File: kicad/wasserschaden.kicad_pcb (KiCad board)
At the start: 2 copper layers, 50.8 x 49.5 mm, 18 parts, among them J1 valve out, J2 12V in, J3 sense, U1 stepdown, U2 WeMos_mini, U3 DS18B20

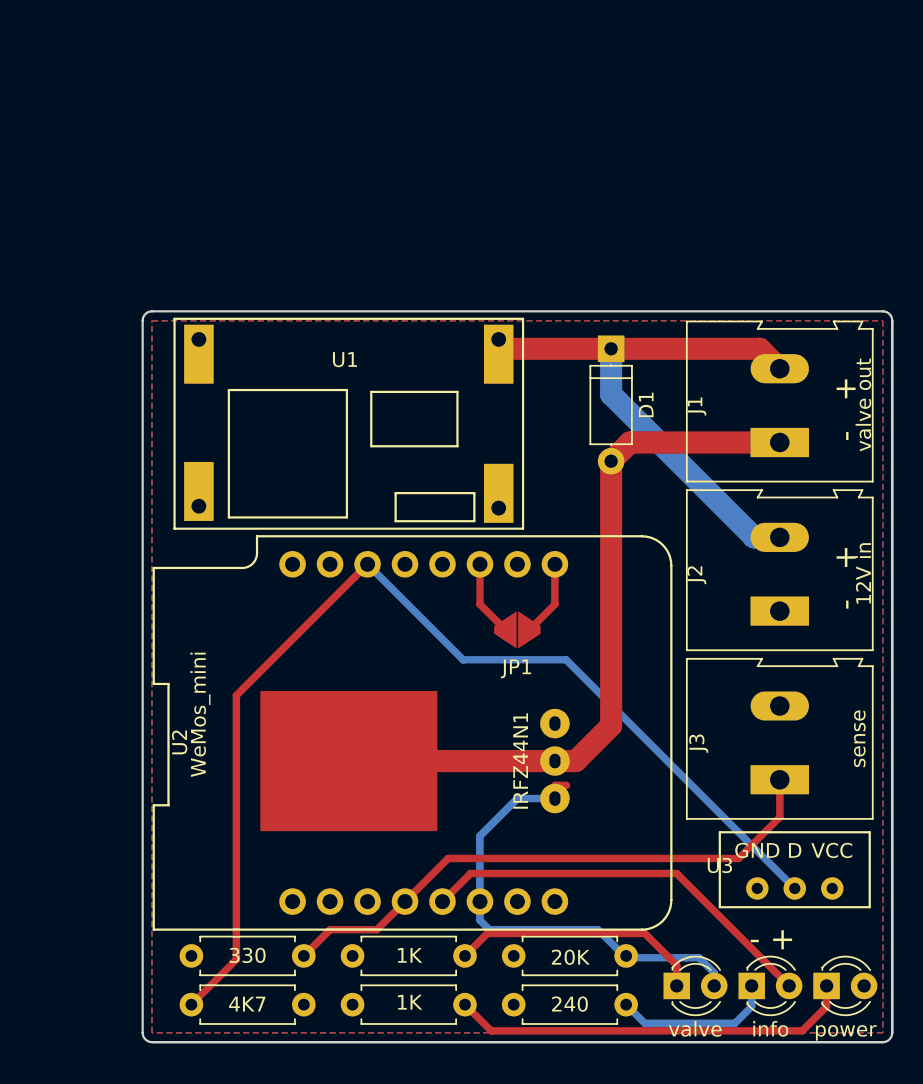
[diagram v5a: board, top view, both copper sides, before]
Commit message: added 12V zone, made screw terminals interlockable
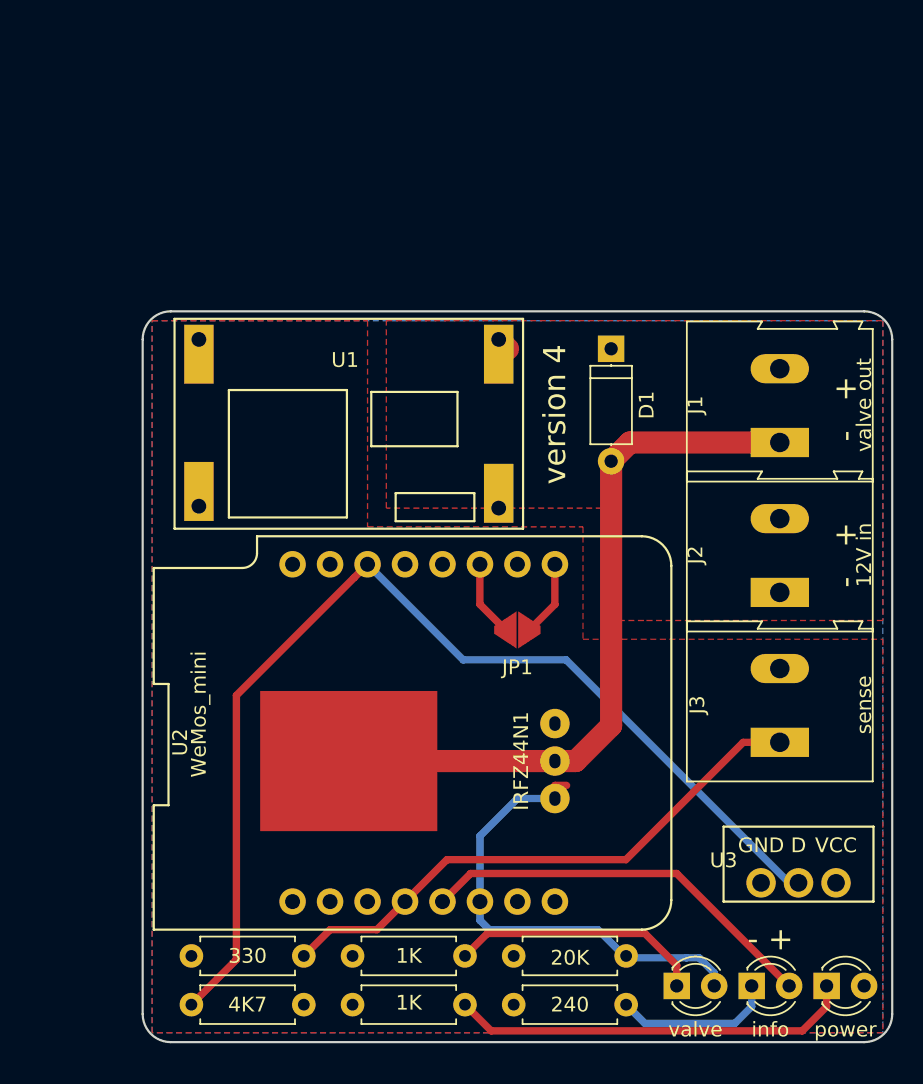
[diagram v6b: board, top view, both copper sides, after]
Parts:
- moved J3 2.54 mm to (168.9, 87.6)
- moved J2 1.27 mm to (168.9, 77.5)
- moved U3 0.46 mm to (170.2, 99.7)
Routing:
- net +12V: track 41.0 -> 3.52 mm
- added copper zone on F.Cu, net +12V
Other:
- outline, holes or cut-outs redrawn
- board text added: "version 4"
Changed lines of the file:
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@@
   (general
     (thickness 1.6)
-    (drawings 13)
-    (tracks 65)
+    (drawings 12)
+    (tracks 59)
     (zones 0)
     (modules 18)
@@
     (mod_text_size 1 1)
     (mod_text_width 0.15)
-    (pad_size 10 12)
-    (pad_drill 3.5)
+    (pad_size 2 2)
+    (pad_drill 1.2)
     (pad_to_mask_clearance 0.2)
     (solder_mask_min_width 0.25)
@@
   )
   (module Connectors_Terminal_Blocks:TerminalBlock_Altech_AK300-2_P5.00mm (layer F.Cu)
-    (at 168.91 78.74 90)
+    (at 168.91 77.47 90)
     (descr "Altech AK300 terminal block, pitch 5.0mm, 45 degree angled, see http://www.mouser.com/ds/2/16/PCBMETRC-24178.pdf")
     (tags "Altech AK300 terminal block pitch 5.0mm")
@@
   )
   (module Connectors_Terminal_Blocks:TerminalBlock_Altech_AK300-2_P5.00mm (layer F.Cu)
-    (at 168.91 90.17 90)
+    (at 168.91 87.63 90)
     (descr "Altech AK300 terminal block, pitch 5.0mm, 45 degree angled, see http://www.mouser.com/ds/2/16/PCBMETRC-24178.pdf")
     (tags "Altech AK300 terminal block pitch 5.0mm")
@@
       (effects (font (size 1 1) (thickness 0.15)))
     )
-    (fp_text value sense (at 2.78 5.334 90) (layer F.SilkS)
+    (fp_text value sense (at 2.54 5.715 90) (layer F.SilkS)
       (effects (font (size 1 1) (thickness 0.15)))
     )
@@
   )
   (module custom:temperature_sensor (layer F.Cu)
-    (at 169.926 100.076)
+    (at 170.18 99.695)
     (fp_text reference U3 (at -5.08 -4.064) (layer F.SilkS)
       (effects (font (size 1 1) (thickness 0.15)))
@@
       (effects (font (size 1 1) (thickness 0.15)))
     )
-    (pad 3 thru_hole circle (at 2.54 -2.54) (size 1.524 1.524) (drill 0.762) (layers *.Cu *.Mask)
+    (pad 3 thru_hole circle (at 2.54 -2.54) (size 2 2) (drill 1.2) (layers *.Cu *.Mask)
       (net 17 +3V3))
-    (pad 2 thru_hole circle (at 0 -2.54) (size 1.524 1.524) (drill 0.762) (layers *.Cu *.Mask)
+    (pad 2 thru_hole circle (at 0 -2.54) (size 2 2) (drill 1.2) (layers *.Cu *.Mask)
       (net 21 "Net-(R6-Pad2)"))
-    (pad 1 thru_hole circle (at -2.54 -2.54) (size 1.524 1.524) (drill 0.762) (layers *.Cu *.Mask)
+    (pad 1 thru_hole circle (at -2.54 -2.54) (size 2 2) (drill 1.2) (layers *.Cu *.Mask)
       (net 3 GND))
   )
-  (gr_arc (start 175.895 107.315) (end 176.53 107.315) (angle 90) (layer Edge.Cuts) (width 0.15))
-  (gr_text "- +" (at 168.402 100.965) (layer F.SilkS)
+  (gr_arc (start 127.635 106.045) (end 125.73 106.045) (angle -90) (layer Edge.Cuts) (width 0.15))
+  (gr_arc (start 174.625 106.045) (end 174.625 107.95) (angle -90) (layer Edge.Cuts) (width 0.15))
+  (gr_arc (start 174.625 60.325) (end 176.53 60.325) (angle -90) (layer Edge.Cuts) (width 0.15))
+  (gr_arc (start 127.635 60.325) (end 127.635 58.42) (angle -90) (layer Edge.Cuts) (width 0.15))
+  (gr_text "version 4" (at 153.67 65.405 90) (layer F.SilkS)
+    (effects (font (size 1.5 1.5) (thickness 0.3)))
+  )
+  (gr_text "- +" (at 168.275 100.965) (layer F.SilkS)
     (effects (font (size 1.5 1.5) (thickness 0.3)))
   )
@@
     (effects (font (size 1.5 1.5) (thickness 0.3)))
   )
-  (gr_text "-   +" (at 173.355 76.454 90) (layer F.SilkS)
+  (gr_text "-   +" (at 173.355 74.93 90) (layer F.SilkS)
     (effects (font (size 1.5 1.5) (thickness 0.3)))
   )
-  (gr_line (start 175.895 107.95) (end 126.365 107.95) (angle 90) (layer Edge.Cuts) (width 0.15))
-  (gr_arc (start 126.365 107.315) (end 126.365 107.95) (angle 90) (layer Edge.Cuts) (width 0.15))
-  (gr_line (start 126.365 107.95) (end 175.895 107.95) (angle 90) (layer Edge.Cuts) (width 0.15))
-  (gr_line (start 176.53 59.055) (end 176.53 107.315) (angle 90) (layer Edge.Cuts) (width 0.15))
-  (gr_arc (start 126.365 59.055) (end 125.73 59.055) (angle 90) (layer Edge.Cuts) (width 0.15))
-  (gr_arc (start 175.895 59.055) (end 175.895 58.42) (angle 90) (layer Edge.Cuts) (width 0.15))
-  (gr_line (start 175.895 58.42) (end 126.365 58.42) (angle 90) (layer Edge.Cuts) (width 0.15))
-  (gr_line (start 176.53 59.055) (end 176.53 107.315) (angle 90) (layer Edge.Cuts) (width 0.15))
-  (gr_line (start 125.73 59.055) (end 125.73 107.315) (angle 90) (layer Edge.Cuts) (width 0.15))
-  (segment (start 157.48 60.96) (end 157.48 64.06) (width 1.5) (layer B.Cu) (net 1))
-  (segment (start 157.48 64.06) (end 167.16 73.74) (width 1.5) (layer B.Cu) (net 1))
-  (segment (start 167.16 73.74) (end 168.91 73.74) (width 1.5) (layer B.Cu) (net 1))
-  (segment (start 167.56 60.96) (end 168.91 62.31) (width 1.5) (layer F.Cu) (net 1))
-  (segment (start 157.48 60.96) (end 167.56 60.96) (width 1.5) (layer F.Cu) (net 1))
+  (gr_line (start 174.625 107.95) (end 127.635 107.95) (angle 90) (layer Edge.Cuts) (width 0.15))
+  (gr_line (start 174.625 58.42) (end 127.635 58.42) (angle 90) (layer Edge.Cuts) (width 0.15))
+  (gr_line (start 176.53 60.325) (end 176.53 106.045) (angle 90) (layer Edge.Cuts) (width 0.15))
+  (gr_line (start 125.73 60.325) (end 125.73 106.045) (angle 90) (layer Edge.Cuts) (width 0.15))
   (segment (start 149.86 60.325) (end 149.86 62.23) (width 0.5) (layer F.Cu) (net 1))
   (segment (start 150.368 60.96) (end 149.86 60.452) (width 1.5) (layer F.Cu) (net 1))
   (segment (start 150.495 60.96) (end 149.86 60.325) (width 1.5) (layer F.Cu) (net 1))
-  (segment (start 157.48 60.96) (end 150.495 60.96) (width 1.5) (layer F.Cu) (net 1))
   (segment (start 158.75 67.31) (end 157.48 68.58) (width 1.5) (layer F.Cu) (net 2))
   (segment (start 168.91 67.31) (end 158.75 67.31) (width 1.5) (layer F.Cu) (net 2))
@@
   (segment (start 153.67 78.2828) (end 153.67 75.565) (width 0.5) (layer F.Cu) (net 19))
   (segment (start 151.9428 80.01) (end 153.67 78.2828) (width 0.5) (layer F.Cu) (net 19))
-  (segment (start 168.91 90.17) (end 168.91 92.71) (width 0.5) (layer F.Cu) (net 20))
-  (segment (start 143.51 98.425) (end 146.431 95.504) (width 0.5) (layer F.Cu) (net 20))
-  (segment (start 166.116 95.504) (end 168.91 92.71) (width 0.5) (layer F.Cu) (net 20))
-  (segment (start 146.431 95.504) (end 166.116 95.504) (width 0.5) (layer F.Cu) (net 20))
   (segment (start 143.51 98.425) (end 141.605 100.33) (width 0.5) (layer F.Cu) (net 20))
   (segment (start 141.605 100.33) (end 138.43 100.33) (width 0.5) (layer F.Cu) (net 20))
   (segment (start 138.43 100.33) (end 136.652 102.108) (width 0.5) (layer F.Cu) (net 20))
+  (segment (start 166.43 87.63) (end 168.91 87.63) (width 0.5) (layer F.Cu) (net 20))
+  (segment (start 158.475001 95.584999) (end 166.43 87.63) (width 0.5) (layer F.Cu) (net 20))
+  (segment (start 146.350001 95.584999) (end 158.475001 95.584999) (width 0.5) (layer F.Cu) (net 20))
+  (segment (start 143.51 98.425) (end 146.350001 95.584999) (width 0.5) (layer F.Cu) (net 20))
   (segment (start 169.926 97.536) (end 154.432 82.042) (width 0.5) (layer B.Cu) (net 21))
   (segment (start 147.447 82.042) (end 154.432 82.042) (width 0.5) (layer B.Cu) (net 21))
@@
     (polygon
       (pts
-        (xy 126.365 59.055) (xy 175.895 59.055) (xy 175.895 107.315) (xy 126.365 107.315)
+        (xy 126.365 59.055) (xy 140.97 59.055) (xy 140.97 73.025) (xy 155.575 73.025) (xy 155.575 80.645)
+        (xy 175.895 80.645) (xy 175.895 107.315) (xy 126.365 107.315)
       )
     )
@@
       )
     )
+  )
+  (zone (net 1) (net_name +12V) (layer F.Cu) (hatch edge 0.508)
+    (connect_pads (clearance 0.508))
+    (min_thickness 0.254)
+    (fill yes (arc_segments 16) (thermal_gap 0.508) (thermal_bridge_width 0.508))
+    (polygon
+      (pts
+        (xy 142.24 59.055) (xy 175.895 59.055) (xy 175.895 79.375) (xy 159.7025 79.375) (xy 156.845 79.375)
+        (xy 156.845 71.755) (xy 142.24 71.755)
+      )
+    )

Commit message: v4 export
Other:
- board text added: "4"
- board text added: "made by humans on earth"
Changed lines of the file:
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@@
   (general
     (thickness 1.6)
-    (drawings 12)
+    (drawings 14)
     (tracks 59)
     (zones 0)
@@
     (add_net "Net-(D1-Pad2)")
   )
+  (module custom:temperature_sensor (layer F.Cu)
+    (at 170.18 99.695)
+    (fp_text reference U3 (at -5.08 -4.064) (layer F.SilkS)
+      (effects (font (size 1 1) (thickness 0.15)))
+    )
+    (fp_text value DS18B20 (at 0 -0.5) (layer F.Fab)
+      (effects (font (size 1 1) (thickness 0.15)))
+    )
+    (fp_line (start -5.08 -1.27) (end -5.08 -6.35) (layer F.SilkS) (width 0.15))
+    (fp_line (start 5.08 -1.27) (end -5.08 -1.27) (layer F.SilkS) (width 0.15))
+    (fp_line (start 5.08 -6.35) (end 5.08 -1.27) (layer F.SilkS) (width 0.15))
+    (fp_line (start -5.08 -6.35) (end 5.08 -6.35) (layer F.SilkS) (width 0.15))
+    (fp_text user VCC (at 2.54 -5.08) (layer F.SilkS)
+      (effects (font (size 1 1) (thickness 0.15)))
+    )
+    (fp_text user D (at 0 -5.08) (layer F.SilkS)
+      (effects (font (size 1 1) (thickness 0.15)))
+    )
+    (fp_text user GND (at -2.54 -5.08) (layer F.SilkS)
+      (effects (font (size 1 1) (thickness 0.15)))
+    )
+    (pad 3 thru_hole circle (at 3.048 -2.54) (size 2 2) (drill 1.2) (layers *.Cu *.Mask)
+      (net 17 +3V3))
+    (pad 2 thru_hole circle (at 0 -2.54) (size 2 2) (drill 1.2) (layers *.Cu *.Mask)
+      (net 21 "Net-(R6-Pad2)"))
+    (pad 1 thru_hole circle (at -3.048 -2.54) (size 2 2) (drill 1.2) (layers *.Cu *.Mask)
+      (net 3 GND))
+  )
   (module custom:wemos (layer F.Cu)
     (at 144.78 86.995)
@@
     )
   )
-  (module custom:temperature_sensor (layer F.Cu)
-    (at 170.18 99.695)
-    (fp_text reference U3 (at -5.08 -4.064) (layer F.SilkS)
-      (effects (font (size 1 1) (thickness 0.15)))
-    )
-    (fp_text value DS18B20 (at 0 -0.5) (layer F.Fab)
-      (effects (font (size 1 1) (thickness 0.15)))
-    )
-    (fp_line (start -5.08 -1.27) (end -5.08 -6.35) (layer F.SilkS) (width 0.15))
-    (fp_line (start 5.08 -1.27) (end -5.08 -1.27) (layer F.SilkS) (width 0.15))
-    (fp_line (start 5.08 -6.35) (end 5.08 -1.27) (layer F.SilkS) (width 0.15))
-    (fp_line (start -5.08 -6.35) (end 5.08 -6.35) (layer F.SilkS) (width 0.15))
-    (fp_text user VCC (at 2.54 -5.08) (layer F.SilkS)
-      (effects (font (size 1 1) (thickness 0.15)))
-    )
-    (fp_text user D (at 0 -5.08) (layer F.SilkS)
-      (effects (font (size 1 1) (thickness 0.15)))
-    )
-    (fp_text user GND (at -2.54 -5.08) (layer F.SilkS)
-      (effects (font (size 1 1) (thickness 0.15)))
-    )
-    (pad 3 thru_hole circle (at 2.54 -2.54) (size 2 2) (drill 1.2) (layers *.Cu *.Mask)
-      (net 17 +3V3))
-    (pad 2 thru_hole circle (at 0 -2.54) (size 2 2) (drill 1.2) (layers *.Cu *.Mask)
-      (net 21 "Net-(R6-Pad2)"))
-    (pad 1 thru_hole circle (at -2.54 -2.54) (size 2 2) (drill 1.2) (layers *.Cu *.Mask)
-      (net 3 GND))
+  (gr_text 4 (at 152.4 86.36) (layer B.SilkS)
+    (effects (font (size 40 45) (thickness 5)) (justify mirror))
+  )
+  (gr_text "made by humans on earth" (at 173.99 74.93 90) (layer B.SilkS)
+    (effects (font (size 1.5 1.5) (thickness 0.3)) (justify mirror))
   )
   (gr_arc (start 127.635 106.045) (end 125.73 106.045) (angle -90) (layer Edge.Cuts) (width 0.15))
@@
   (segment (start 146.350001 95.584999) (end 158.475001 95.584999) (width 0.5) (layer F.Cu) (net 20))
   (segment (start 143.51 98.425) (end 146.350001 95.584999) (width 0.5) (layer F.Cu) (net 20))
-  (segment (start 169.926 97.536) (end 154.432 82.042) (width 0.5) (layer B.Cu) (net 21))
-  (segment (start 147.447 82.042) (end 154.432 82.042) (width 0.5) (layer B.Cu) (net 21))
-  (segment (start 140.97 75.565) (end 147.447 82.042) (width 0.5) (layer B.Cu) (net 21))
   (segment (start 132.08 84.455) (end 140.070001 76.464999) (width 0.5) (layer F.Cu) (net 21))
   (segment (start 132.08 102.362) (end 132.08 84.455) (width 0.5) (layer F.Cu) (net 21))
   (segment (start 140.070001 76.464999) (end 140.97 75.565) (width 0.5) (layer F.Cu) (net 21))
   (segment (start 129.032 105.41) (end 132.08 102.362) (width 0.5) (layer F.Cu) (net 21))
+  (segment (start 140.97 75.565) (end 147.447 82.042) (width 0.5) (layer B.Cu) (net 21))
+  (segment (start 155.067 82.042) (end 170.18 97.155) (width 0.5) (layer B.Cu) (net 21))
+  (segment (start 147.447 82.042) (end 155.067 82.042) (width 0.5) (layer B.Cu) (net 21))
   (zone (net 17) (net_name +3V3) (layer F.Cu) (hatch edge 0.508)
     (connect_pads (clearance 0.508))

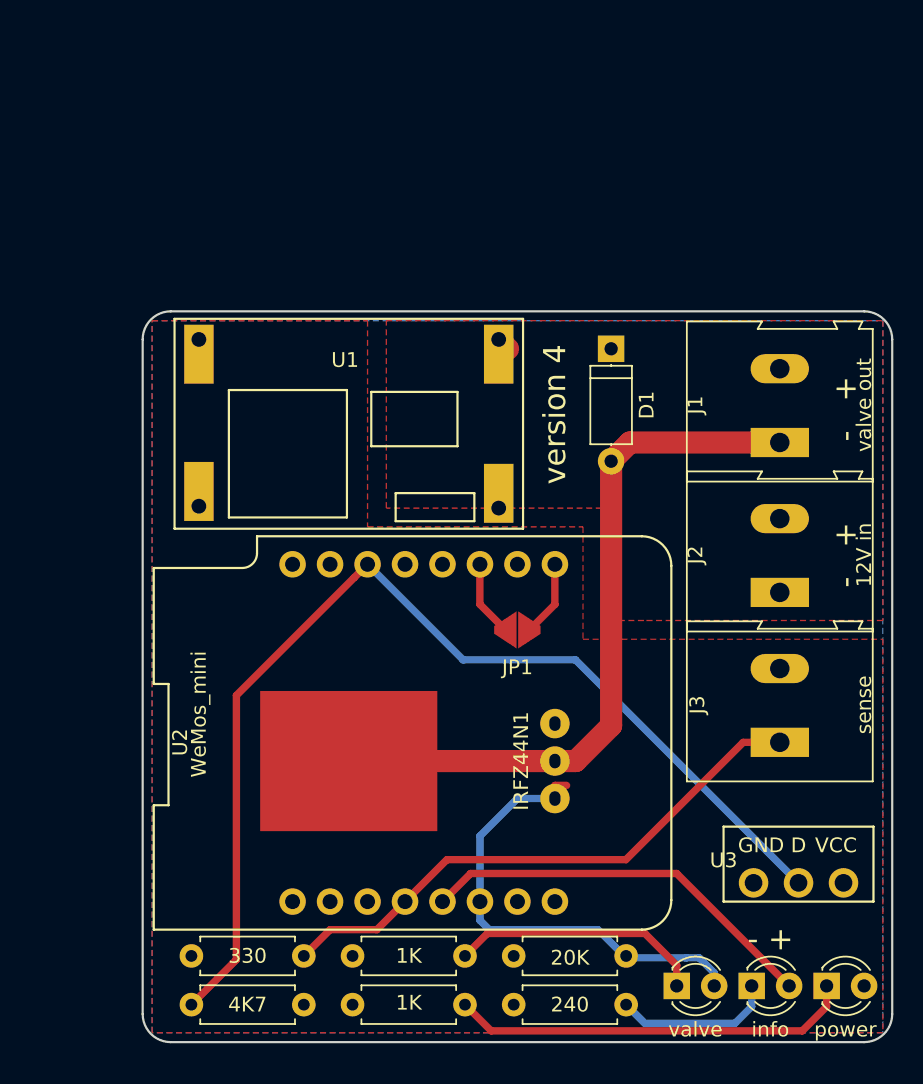
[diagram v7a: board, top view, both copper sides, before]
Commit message: cleaned up old files and replaced main pcb with smd version
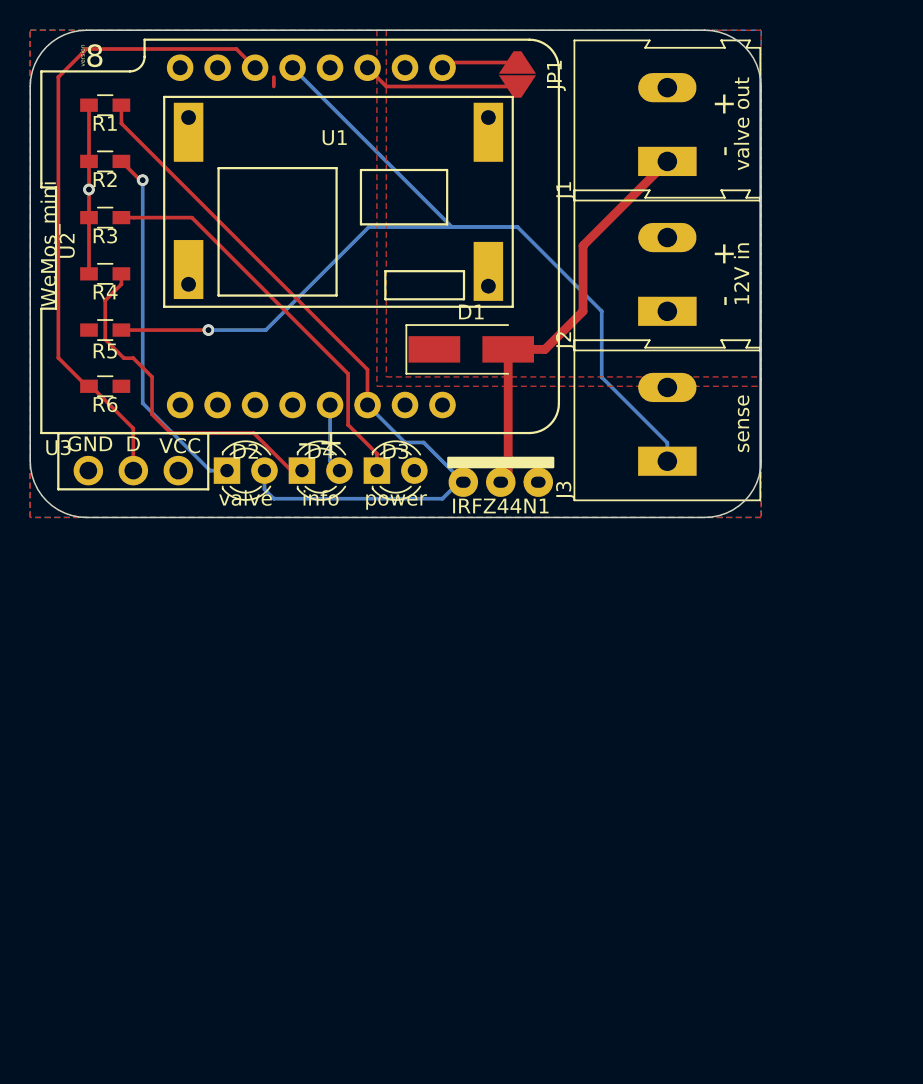
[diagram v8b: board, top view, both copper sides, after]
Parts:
- added ?: , , F.Cu at (29.8, -2.54)
- D1: footprint Diodes_THT:D_A-405_P7.62mm_Horizontal -> Diodes_SMD:D_SMA_Handsoldering
- D3: value power -> LED
- IRFZ44N1: footprint custom:irlz44n -> custom:irlz44n_vertical
- R1, R2, R3, R4, R5, R6: footprint Resistors_THT:R_Axial_DIN0207_L6.3mm_D2.5mm_P7.62mm_Horizontal -> Resistors_SMD:R_0603_HandSoldering
- moved R1 64.0 mm to (123.2, 44.5)
- moved R3 58.6 mm to (123.2, 52.1)
- moved R4 56.7 mm to (123.2, 55.9)
- moved R2 56.4 mm to (123.2, 48.3)
- moved U3 53.0 mm to (125.1, 71.8)
- moved D2 46.4 mm to (131.4, 69.2)
- moved D3 46.4 mm to (141.6, 69.2)
- moved D4 46.4 mm to (136.5, 69.2)
- moved R5 44.5 mm to (123.2, 59.7)
- moved R6 44.0 mm to (123.2, 63.5)
- moved JP1 37.6 mm to (151.1, 42.4), turned to 90 degrees
- moved U2 34.5 mm to (137.2, 53.3)
- moved J1 20.5 mm to (161.3, 48.3)
- moved J2 20.5 mm to (161.3, 58.4)
- moved J3 20.5 mm to (161.3, 68.6)
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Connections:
- U2 pad 13: Net-(U2-Pad13) -> Net-(J3-Pad1)
- U2 pad 4: Net-(J3-Pad1) -> Net-(U2-Pad4)
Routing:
- net Net-(R6-Pad2): track 72.9 -> 43.6 mm
- net Net-(J3-Pad1): track 38.3 -> 65.1 mm, vias 0 -> 1
- net Net-(D4-Pad2): track 27.4 -> 4.71 mm
- net Net-(D1-Pad2): track 48.7 -> 27.9 mm
- net Net-(D2-Pad2): track 32.4 -> 51.1 mm
- net Net-(D4-Pad1): track 10.9 -> 23.4 mm
- net GND: track 3.81 -> 11.4 mm, vias 0 -> 1
- net Net-(D2-Pad1): track 17.3 -> 24.5 mm, vias 0 -> 1
- net Net-(JP1-Pad1): track 5.16 -> 10.7 mm
- net +12V: track 3.52 -> 0.00 mm
- net +3V3: track 1.90 -> 0.88 mm
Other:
- board size 50.8 x 49.5 mm -> 49.5 x 33 mm
- net class Default: trace_width 0.5 -> 0.25; via_dia 0.6 -> 0.8
- net class more added: clearance 0.4, trace_width 0.6, via_dia 0.8, via_drill 0.4
- net class power removed
- rule pad_to_mask_clearance: 0.2 -> 0
- board text added: "8"
- board text added: "info"
- board text added: "power"
- board text added: "valve"
- board text added: "version"
- board text removed: "4"
- board text removed: "made by humans on earth"
- board text removed: "version 4"
